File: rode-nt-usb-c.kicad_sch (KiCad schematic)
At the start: 5 parts, among them J1 USB_C_Receptacle, J2 Conn_01x05_Pin

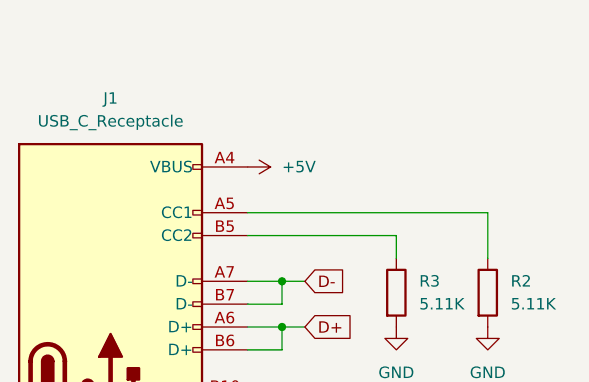
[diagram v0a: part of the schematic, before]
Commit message: Change routing
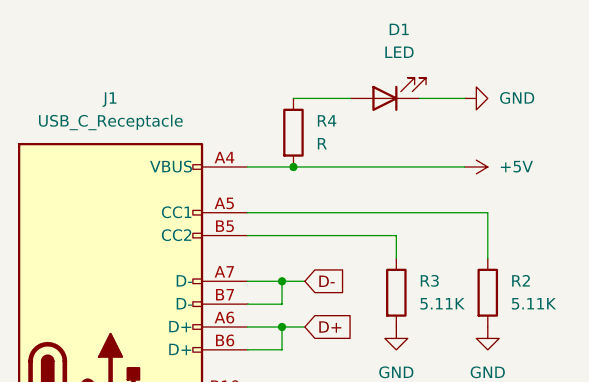
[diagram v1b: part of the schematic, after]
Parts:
- added D1: LED, LED_SMD:LED_1206_3216Metric_Pad1.42x1.75mm_HandSolder, symbol Device:LED
- added R4: R, Resistor_SMD:R_1206_3216Metric_Pad1.30x1.75mm_HandSolder, symbol Device:R
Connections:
- net +5V: now also R4.2
- net GND: now also D1.1 (K)
- new net: D1.2 (A), R4.1
